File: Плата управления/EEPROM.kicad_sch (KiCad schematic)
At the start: 2 parts, among them U1 AT25xxx

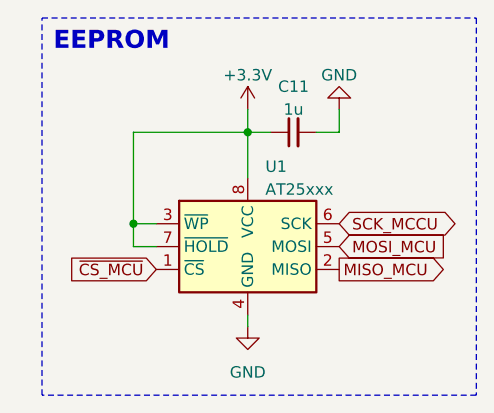
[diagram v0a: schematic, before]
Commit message: Заменил разъём под силовую плату
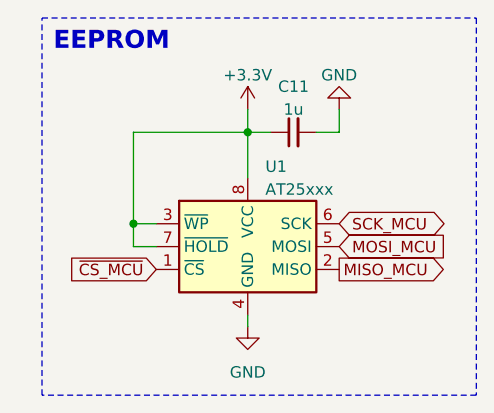
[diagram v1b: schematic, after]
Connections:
- net SCK_MCCU renamed SCK_MCU
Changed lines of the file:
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@@
     )
   )
-  (global_label "SCK_MCCU" (shape bidirectional) (at 48.26 38.1 0) (fields_autoplaced)
+  (global_label "SCK_MCU" (shape bidirectional) (at 48.26 38.1 0) (fields_autoplaced)
     (effects (font (size 1.27 1.27)) (justify left))
-    (property "Intersheetrefs" "${INTERSHEET_REFS}" (at 62.3161 38.1 0)
+    (property "Intersheetrefs" "${INTERSHEET_REFS}" (at 61.0461 38.1 0)
       (effects (font (size 1.27 1.27)) (justify left) hide)
     )

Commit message: Редактировал схему
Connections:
- net MISO_MCU renamed EEPROM_MISO_MCU
- net MOSI_MCU renamed EEPROM_MOSI_MCU
- net SCK_MCU renamed EEPROM_SCK_MCU
- net ~{CS_MCU} renamed EEPROM_~{CS_MCU}
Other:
- moved on the sheet: C11, U1
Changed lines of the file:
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@@
 (kicad_sch (version 20230121) (generator eeschema)
   (paper "A4")
-  (junction (at 25.4 38.1) (diameter 0) (color 0 0 0 0)
+  (junction (at 34.29 38.1) (diameter 0) (color 0 0 0 0)
   )
-  (junction (at 38.1 27.94) (diameter 0) (color 0 0 0 0)
+  (junction (at 46.99 27.94) (diameter 0) (color 0 0 0 0)
   )
-  (wire (pts (xy 38.1 33.02) (xy 38.1 27.94))
+  (wire (pts (xy 46.99 33.02) (xy 46.99 27.94))
     (stroke (width 0) (type default))
   )
-  (wire (pts (xy 25.4 27.94) (xy 38.1 27.94))
+  (wire (pts (xy 34.29 27.94) (xy 46.99 27.94))
     (stroke (width 0) (type default))
   )
-  (wire (pts (xy 38.1 27.94) (xy 40.64 27.94))
+  (wire (pts (xy 46.99 27.94) (xy 49.53 27.94))
     (stroke (width 0) (type default))
   )
-  (wire (pts (xy 38.1 25.4) (xy 38.1 27.94))
+  (wire (pts (xy 46.99 25.4) (xy 46.99 27.94))
     (stroke (width 0) (type default))
   )
-  (wire (pts (xy 45.72 27.94) (xy 48.26 27.94))
+  (wire (pts (xy 54.61 27.94) (xy 57.15 27.94))
     (stroke (width 0) (type default))
   )
-  (wire (pts (xy 25.4 40.64) (xy 25.4 38.1))
+  (wire (pts (xy 34.29 40.64) (xy 34.29 38.1))
     (stroke (width 0) (type default))
   )
-  (wire (pts (xy 27.94 40.64) (xy 25.4 40.64))
+  (wire (pts (xy 36.83 40.64) (xy 34.29 40.64))
     (stroke (width 0) (type default))
   )
-  (wire (pts (xy 25.4 38.1) (xy 27.94 38.1))
+  (wire (pts (xy 34.29 38.1) (xy 36.83 38.1))
     (stroke (width 0) (type default))
   )
-  (wire (pts (xy 25.4 38.1) (xy 25.4 27.94))
+  (wire (pts (xy 34.29 38.1) (xy 34.29 27.94))
     (stroke (width 0) (type default))
   )
-  (wire (pts (xy 38.1 48.26) (xy 38.1 49.53))
+  (wire (pts (xy 46.99 48.26) (xy 46.99 49.53))
     (stroke (width 0) (type default))
   )
-  (wire (pts (xy 48.26 27.94) (xy 48.26 25.4))
+  (wire (pts (xy 57.15 27.94) (xy 57.15 25.4))
     (stroke (width 0) (type default))
   )
-  (rectangle (start 15.24 15.24) (end 63.5 57.15)
+  (rectangle (start 15.24 15.24) (end 80.01 57.15)
     (stroke (width 0) (type dot))
     (fill (type none))
@@
     (effects (font (size 2 2) (thickness 0.4) bold) (justify left bottom))
   )
-  (global_label "MISO_MCU" (shape output) (at 48.26 43.18 0) (fields_autoplaced)
+  (global_label "EEPROM_MISO_MCU" (shape output) (at 57.15 43.18 0) (fields_autoplaced)
     (effects (font (size 1.27 1.27)) (justify left))
-    (property "Intersheetrefs" "${INTERSHEET_REFS}" (at 60.7815 43.18 0)
+    (property "Intersheetrefs" "${INTERSHEET_REFS}" (at 78.3384 43.18 0)
       (effects (font (size 1.27 1.27)) (justify left) hide)
     )
   )
-  (global_label "~{CS_MCU}" (shape input) (at 27.94 43.18 180) (fields_autoplaced)
+  (global_label "EEPROM_~{CS_MCU}" (shape input) (at 36.83 43.18 180) (fields_autoplaced)
     (effects (font (size 1.27 1.27)) (justify right))
-    (property "Intersheetrefs" "${INTERSHEET_REFS}" (at 17.5352 43.18 0)
+    (property "Intersheetrefs" "${INTERSHEET_REFS}" (at 17.7583 43.18 0)
       (effects (font (size 1.27 1.27)) (justify right) hide)
     )
   )
-  (global_label "SCK_MCU" (shape bidirectional) (at 48.26 38.1 0) (fields_autoplaced)
+  (global_label "EEPROM_SCK_MCU" (shape bidirectional) (at 57.15 38.1 0) (fields_autoplaced)
     (effects (font (size 1.27 1.27)) (justify left))
-    (property "Intersheetrefs" "${INTERSHEET_REFS}" (at 61.0461 38.1 0)
+    (property "Intersheetrefs" "${INTERSHEET_REFS}" (at 78.603 38.1 0)
       (effects (font (size 1.27 1.27)) (justify left) hide)
     )
   )
-  (global_label "MOSI_MCU" (shape input) (at 48.26 40.64 0) (fields_autoplaced)
+  (global_label "EEPROM_MOSI_MCU" (shape input) (at 57.15 40.64 0) (fields_autoplaced)
     (effects (font (size 1.27 1.27)) (justify left))
-    (property "Intersheetrefs" "${INTERSHEET_REFS}" (at 60.7815 40.64 0)
+    (property "Intersheetrefs" "${INTERSHEET_REFS}" (at 78.3384 40.64 0)
       (effects (font (size 1.27 1.27)) (justify left) hide)
     )
   )
-  (symbol (lib_id "Device:C_Small") (at 43.18 27.94 90) (unit 1)
+  (symbol (lib_id "Device:C_Small") (at 52.07 27.94 90) (unit 1)
     (in_bom yes) (on_board yes) (dnp no) (fields_autoplaced)
-    (property "Reference" "C11" (at 43.1863 22.86 90)
+    (property "Reference" "C11" (at 52.0763 22.86 90)
       (effects (font (size 1.27 1.27)))
     )
-    (property "Value" "1u" (at 43.1863 25.4 90)
+    (property "Value" "1u" (at 52.0763 25.4 90)
       (effects (font (size 1.27 1.27)))
     )
-    (property "Footprint" "Capacitor_SMD:C_0603_1608Metric_Pad1.08x0.95mm_HandSolder" (at 43.18 27.94 0)
+    (property "Footprint" "Capacitor_SMD:C_0603_1608Metric_Pad1.08x0.95mm_HandSolder" (at 52.07 27.94 0)
       (effects (font (size 1.27 1.27)) hide)
     )
-    (property "Datasheet" "~" (at 43.18 27.94 0)
+    (property "Datasheet" "~" (at 52.07 27.94 0)
       (effects (font (size 1.27 1.27)) hide)
     )
@@
     )
   )
-  (symbol (lib_id "power:GND") (at 38.1 49.53 0) (unit 1)
+  (symbol (lib_id "power:GND") (at 46.99 49.53 0) (unit 1)
     (in_bom yes) (on_board yes) (dnp no) (fields_autoplaced)
-    (property "Reference" "#PWR0108" (at 38.1 55.88 0)
+    (property "Reference" "#PWR0108" (at 46.99 55.88 0)
       (effects (font (size 1.27 1.27)) hide)
     )
-    (property "Value" "GND" (at 38.1 54.61 0)
+    (property "Value" "GND" (at 46.99 54.61 0)
       (effects (font (size 1.27 1.27)))
     )
-    (property "Footprint" "" (at 38.1 49.53 0)
+    (property "Footprint" "" (at 46.99 49.53 0)
       (effects (font (size 1.27 1.27)) hide)
     )
-    (property "Datasheet" "" (at 38.1 49.53 0)
+    (property "Datasheet" "" (at 46.99 49.53 0)
       (effects (font (size 1.27 1.27)) hide)
     )
@@
     )
   )
-  (symbol (lib_id "Memory_EEPROM:AT25xxx") (at 38.1 40.64 0) (unit 1)
+  (symbol (lib_id "Memory_EEPROM:AT25xxx") (at 46.99 40.64 0) (unit 1)
     (in_bom yes) (on_board yes) (dnp no) (fields_autoplaced)
-    (property "Reference" "U1" (at 40.0559 31.75 0)
+    (property "Reference" "U1" (at 48.9459 31.75 0)
       (effects (font (size 1.27 1.27)) (justify left))
     )
-    (property "Value" "AT25xxx" (at 40.0559 34.29 0)
+    (property "Value" "AT25xxx" (at 48.9459 34.29 0)
       (effects (font (size 1.27 1.27)) (justify left))
     )
-    (property "Footprint" "Package_SO:SOIC-8_3.9x4.9mm_P1.27mm" (at 38.1 40.64 0)
+    (property "Footprint" "Package_SO:SOIC-8_3.9x4.9mm_P1.27mm" (at 46.99 40.64 0)
       (effects (font (size 1.27 1.27)) hide)
     )
-    (property "Datasheet" "http://ww1.microchip.com/downloads/en/DeviceDoc/Atmel-8707-SEEPROM-AT25010B-020B-040B-Datasheet.pdf" (at 38.1 40.64 0)
+    (property "Datasheet" "http://ww1.microchip.com/downloads/en/DeviceDoc/Atmel-8707-SEEPROM-AT25010B-020B-040B-Datasheet.pdf" (at 46.99 40.64 0)
       (effects (font (size 1.27 1.27)) hide)
     )
@@
     )
   )
-  (symbol (lib_id "power:+3.3V") (at 38.1 25.4 0) (unit 1)
+  (symbol (lib_id "power:+3.3V") (at 46.99 25.4 0) (unit 1)
     (in_bom yes) (on_board yes) (dnp no) (fields_autoplaced)
-    (property "Reference" "#PWR0110" (at 38.1 29.21 0)
+    (property "Reference" "#PWR0110" (at 46.99 29.21 0)
       (effects (font (size 1.27 1.27)) hide)
     )
-    (property "Value" "+3.3V" (at 38.1 21.59 0)
+    (property "Value" "+3.3V" (at 46.99 21.59 0)
       (effects (font (size 1.27 1.27)))
     )
-    (property "Footprint" "" (at 38.1 25.4 0)
+    (property "Footprint" "" (at 46.99 25.4 0)
       (effects (font (size 1.27 1.27)) hide)
     )
-    (property "Datasheet" "" (at 38.1 25.4 0)
+    (property "Datasheet" "" (at 46.99 25.4 0)
       (effects (font (size 1.27 1.27)) hide)
     )
@@
     )
   )
-  (symbol (lib_id "power:GND") (at 48.26 25.4 180) (unit 1)
+  (symbol (lib_id "power:GND") (at 57.15 25.4 180) (unit 1)
     (in_bom yes) (on_board yes) (dnp no) (fields_autoplaced)
-    (property "Reference" "#PWR0109" (at 48.26 19.05 0)
+    (property "Reference" "#PWR0109" (at 57.15 19.05 0)
       (effects (font (size 1.27 1.27)) hide)
     )
-    (property "Value" "GND" (at 48.26 21.59 0)
+    (property "Value" "GND" (at 57.15 21.59 0)
       (effects (font (size 1.27 1.27)))
     )
-    (property "Footprint" "" (at 48.26 25.4 0)
+    (property "Footprint" "" (at 57.15 25.4 0)
       (effects (font (size 1.27 1.27)) hide)
     )
-    (property "Datasheet" "" (at 48.26 25.4 0)
+    (property "Datasheet" "" (at 57.15 25.4 0)
       (effects (font (size 1.27 1.27)) hide)
     )

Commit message: Собираю документацию
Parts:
- U1: value AT25xxx -> FM25W256
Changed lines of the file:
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@@
   (symbol (lib_id "Memory_EEPROM:AT25xxx") (at 46.99 40.64 0) (unit 1)
     (in_bom yes) (on_board yes) (dnp no) (fields_autoplaced)
-    (property "Reference" "U1" (at 48.9459 31.75 0)
+    (property "Reference" "U1" (at 49.1841 30.48 0)
       (effects (font (size 1.27 1.27)) (justify left))
     )
-    (property "Value" "AT25xxx" (at 48.9459 34.29 0)
+    (property "Value" "FM25W256" (at 49.1841 33.02 0)
       (effects (font (size 1.27 1.27)) (justify left))
     )

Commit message: Добавил документы
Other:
- note added: "FRAM"
- note removed: "EEPROM"
- moved on the sheet: C11, U1
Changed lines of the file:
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@@
 (kicad_sch (version 20230121) (generator eeschema)
   (paper "A4")
-  (junction (at 34.29 38.1) (diameter 0) (color 0 0 0 0)
+  (title_block
+    (comment 1 "МПСТ.76721.758764.02.Э3.М")
   )
-  (junction (at 46.99 27.94) (diameter 0) (color 0 0 0 0)
+  (junction (at 147.955 103.505) (diameter 0) (color 0 0 0 0)
   )
-  (wire (pts (xy 46.99 33.02) (xy 46.99 27.94))
+  (junction (at 160.655 93.345) (diameter 0) (color 0 0 0 0)
+  )
+  (wire (pts (xy 160.655 98.425) (xy 160.655 93.345))
     (stroke (width 0) (type default))
   )
-  (wire (pts (xy 34.29 27.94) (xy 46.99 27.94))
+  (wire (pts (xy 147.955 93.345) (xy 160.655 93.345))
     (stroke (width 0) (type default))
   )
-  (wire (pts (xy 46.99 27.94) (xy 49.53 27.94))
+  (wire (pts (xy 160.655 93.345) (xy 163.195 93.345))
     (stroke (width 0) (type default))
   )
-  (wire (pts (xy 46.99 25.4) (xy 46.99 27.94))
+  (wire (pts (xy 160.655 90.805) (xy 160.655 93.345))
     (stroke (width 0) (type default))
   )
-  (wire (pts (xy 54.61 27.94) (xy 57.15 27.94))
+  (wire (pts (xy 168.275 93.345) (xy 170.815 93.345))
     (stroke (width 0) (type default))
   )
-  (wire (pts (xy 34.29 40.64) (xy 34.29 38.1))
+  (wire (pts (xy 147.955 106.045) (xy 147.955 103.505))
     (stroke (width 0) (type default))
   )
-  (wire (pts (xy 36.83 40.64) (xy 34.29 40.64))
+  (wire (pts (xy 150.495 106.045) (xy 147.955 106.045))
     (stroke (width 0) (type default))
   )
-  (wire (pts (xy 34.29 38.1) (xy 36.83 38.1))
+  (wire (pts (xy 147.955 103.505) (xy 150.495 103.505))
     (stroke (width 0) (type default))
   )
-  (wire (pts (xy 34.29 38.1) (xy 34.29 27.94))
+  (wire (pts (xy 147.955 103.505) (xy 147.955 93.345))
     (stroke (width 0) (type default))
   )
-  (wire (pts (xy 46.99 48.26) (xy 46.99 49.53))
+  (wire (pts (xy 160.655 113.665) (xy 160.655 114.935))
     (stroke (width 0) (type default))
   )
-  (wire (pts (xy 57.15 27.94) (xy 57.15 25.4))
+  (wire (pts (xy 170.815 93.345) (xy 170.815 90.805))
     (stroke (width 0) (type default))
   )
-  (rectangle (start 15.24 15.24) (end 80.01 57.15)
-    (stroke (width 0) (type dot))
+  (rectangle (start 128.905 80.645) (end 193.675 122.555)
+    (stroke (width 0) (type dash))
     (fill (type none))
   )
-  (text "EEPROM" (at 16.51 19.05 0)
+  (text "FRAM" (at 130.175 84.455 0)
     (effects (font (size 2 2) (thickness 0.4) bold) (justify left bottom))
   )
-  (global_label "EEPROM_MISO_MCU" (shape output) (at 57.15 43.18 0) (fields_autoplaced)
+  (global_label "EEPROM_MISO_MCU" (shape output) (at 170.815 108.585 0) (fields_autoplaced)
     (effects (font (size 1.27 1.27)) (justify left))
-    (property "Intersheetrefs" "${INTERSHEET_REFS}" (at 78.3384 43.18 0)
+    (property "Intersheetrefs" "${INTERSHEET_REFS}" (at 192.0034 108.585 0)
       (effects (font (size 1.27 1.27)) (justify left) hide)
     )
   )
-  (global_label "EEPROM_~{CS_MCU}" (shape input) (at 36.83 43.18 180) (fields_autoplaced)
+  (global_label "EEPROM_~{CS_MCU}" (shape input) (at 150.495 108.585 180) (fields_autoplaced)
     (effects (font (size 1.27 1.27)) (justify right))
-    (property "Intersheetrefs" "${INTERSHEET_REFS}" (at 17.7583 43.18 0)
+    (property "Intersheetrefs" "${INTERSHEET_REFS}" (at 131.4233 108.585 0)
       (effects (font (size 1.27 1.27)) (justify right) hide)
     )
   )
-  (global_label "EEPROM_SCK_MCU" (shape bidirectional) (at 57.15 38.1 0) (fields_autoplaced)
+  (global_label "EEPROM_SCK_MCU" (shape bidirectional) (at 170.815 103.505 0) (fields_autoplaced)
     (effects (font (size 1.27 1.27)) (justify left))
-    (property "Intersheetrefs" "${INTERSHEET_REFS}" (at 78.603 38.1 0)
+    (property "Intersheetrefs" "${INTERSHEET_REFS}" (at 192.268 103.505 0)
       (effects (font (size 1.27 1.27)) (justify left) hide)
     )
   )
-  (global_label "EEPROM_MOSI_MCU" (shape input) (at 57.15 40.64 0) (fields_autoplaced)
+  (global_label "EEPROM_MOSI_MCU" (shape input) (at 170.815 106.045 0) (fields_autoplaced)
     (effects (font (size 1.27 1.27)) (justify left))
-    (property "Intersheetrefs" "${INTERSHEET_REFS}" (at 78.3384 40.64 0)
+    (property "Intersheetrefs" "${INTERSHEET_REFS}" (at 192.0034 106.045 0)
       (effects (font (size 1.27 1.27)) (justify left) hide)
     )
   )
-  (symbol (lib_id "Device:C_Small") (at 52.07 27.94 90) (unit 1)
+  (symbol (lib_id "Device:C_Small") (at 165.735 93.345 90) (unit 1)
     (in_bom yes) (on_board yes) (dnp no) (fields_autoplaced)
-    (property "Reference" "C11" (at 52.0763 22.86 90)
+    (property "Reference" "C11" (at 165.7413 88.265 90)
       (effects (font (size 1.27 1.27)))
     )
-    (property "Value" "1u" (at 52.0763 25.4 90)
+    (property "Value" "1u" (at 165.7413 90.805 90)
       (effects (font (size 1.27 1.27)))
     )
-    (property "Footprint" "Capacitor_SMD:C_0603_1608Metric_Pad1.08x0.95mm_HandSolder" (at 52.07 27.94 0)
+    (property "Footprint" "Capacitor_SMD:C_0603_1608Metric_Pad1.08x0.95mm_HandSolder" (at 165.735 93.345 0)
       (effects (font (size 1.27 1.27)) hide)
     )
-    (property "Datasheet" "~" (at 52.07 27.94 0)
+    (property "Datasheet" "~" (at 165.735 93.345 0)
       (effects (font (size 1.27 1.27)) hide)
     )
@@
     )
   )
-  (symbol (lib_id "power:GND") (at 46.99 49.53 0) (unit 1)
+  (symbol (lib_id "power:GND") (at 160.655 114.935 0) (unit 1)
     (in_bom yes) (on_board yes) (dnp no) (fields_autoplaced)
-    (property "Reference" "#PWR0108" (at 46.99 55.88 0)
+    (property "Reference" "#PWR0108" (at 160.655 121.285 0)
       (effects (font (size 1.27 1.27)) hide)
     )
-    (property "Value" "GND" (at 46.99 54.61 0)
+    (property "Value" "GND" (at 160.655 120.015 0)
       (effects (font (size 1.27 1.27)))
     )
-    (property "Footprint" "" (at 46.99 49.53 0)
+    (property "Footprint" "" (at 160.655 114.935 0)
       (effects (font (size 1.27 1.27)) hide)
     )
-    (property "Datasheet" "" (at 46.99 49.53 0)
+    (property "Datasheet" "" (at 160.655 114.935 0)
       (effects (font (size 1.27 1.27)) hide)
     )
@@
     )
   )
-  (symbol (lib_id "Memory_EEPROM:AT25xxx") (at 46.99 40.64 0) (unit 1)
+  (symbol (lib_id "Memory_EEPROM:AT25xxx") (at 160.655 106.045 0) (unit 1)
     (in_bom yes) (on_board yes) (dnp no) (fields_autoplaced)
-    (property "Reference" "U1" (at 49.1841 30.48 0)
+    (property "Reference" "U1" (at 162.8491 95.885 0)
       (effects (font (size 1.27 1.27)) (justify left))
     )
-    (property "Value" "FM25W256" (at 49.1841 33.02 0)
+    (property "Value" "FM25W256" (at 162.8491 98.425 0)
       (effects (font (size 1.27 1.27)) (justify left))
     )
-    (property "Footprint" "Package_SO:SOIC-8_3.9x4.9mm_P1.27mm" (at 46.99 40.64 0)
+    (property "Footprint" "Package_SO:SOIC-8_3.9x4.9mm_P1.27mm" (at 160.655 106.045 0)
       (effects (font (size 1.27 1.27)) hide)
     )
-    (property "Datasheet" "http://ww1.microchip.com/downloads/en/DeviceDoc/Atmel-8707-SEEPROM-AT25010B-020B-040B-Datasheet.pdf" (at 46.99 40.64 0)
+    (property "Datasheet" "http://ww1.microchip.com/downloads/en/DeviceDoc/Atmel-8707-SEEPROM-AT25010B-020B-040B-Datasheet.pdf" (at 160.655 106.045 0)
       (effects (font (size 1.27 1.27)) hide)
     )
@@
     )
   )
-  (symbol (lib_id "power:+3.3V") (at 46.99 25.4 0) (unit 1)
+  (symbol (lib_id "power:+3.3V") (at 160.655 90.805 0) (unit 1)
     (in_bom yes) (on_board yes) (dnp no) (fields_autoplaced)
-    (property "Reference" "#PWR0110" (at 46.99 29.21 0)
+    (property "Reference" "#PWR0110" (at 160.655 94.615 0)
       (effects (font (size 1.27 1.27)) hide)
     )
-    (property "Value" "+3.3V" (at 46.99 21.59 0)
+    (property "Value" "+3.3V" (at 160.655 86.995 0)
       (effects (font (size 1.27 1.27)))
     )
-    (property "Footprint" "" (at 46.99 25.4 0)
+    (property "Footprint" "" (at 160.655 90.805 0)
       (effects (font (size 1.27 1.27)) hide)
     )
-    (property "Datasheet" "" (at 46.99 25.4 0)
+    (property "Datasheet" "" (at 160.655 90.805 0)
       (effects (font (size 1.27 1.27)) hide)
     )
@@
     )
   )
-  (symbol (lib_id "power:GND") (at 57.15 25.4 180) (unit 1)
+  (symbol (lib_id "power:GND") (at 170.815 90.805 180) (unit 1)
     (in_bom yes) (on_board yes) (dnp no) (fields_autoplaced)
-    (property "Reference" "#PWR0109" (at 57.15 19.05 0)
+    (property "Reference" "#PWR0109" (at 170.815 84.455 0)
       (effects (font (size 1.27 1.27)) hide)
     )
-    (property "Value" "GND" (at 57.15 21.59 0)
+    (property "Value" "GND" (at 170.815 86.995 0)
       (effects (font (size 1.27 1.27)))
     )
-    (property "Footprint" "" (at 57.15 25.4 0)
+    (property "Footprint" "" (at 170.815 90.805 0)
       (effects (font (size 1.27 1.27)) hide)
     )
-    (property "Datasheet" "" (at 57.15 25.4 0)
+    (property "Datasheet" "" (at 170.815 90.805 0)
       (effects (font (size 1.27 1.27)) hide)
     )

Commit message: Добавил все документы
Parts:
- renumbered C11 to C54, U1 to U12
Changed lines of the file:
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@@
   (symbol (lib_id "Device:C_Small") (at 165.735 93.345 90) (unit 1)
     (in_bom yes) (on_board yes) (dnp no) (fields_autoplaced)
-    (property "Reference" "C11" (at 165.7413 88.265 90)
+    (property "Reference" "C54" (at 165.7413 88.265 90)
       (effects (font (size 1.27 1.27)))
     )
@@
       (project "Плата управления"
         (path "/75f4c67c-bbde-4446-8f82-67797a1b269f/bbae964f-aef3-47b6-89c5-594b5cc7787c"
-          (reference "C11") (unit 1)
+          (reference "C54") (unit 1)
         )
       )
@@
   (symbol (lib_id "power:GND") (at 160.655 114.935 0) (unit 1)
     (in_bom yes) (on_board yes) (dnp no) (fields_autoplaced)
-    (property "Reference" "#PWR0108" (at 160.655 121.285 0)
+    (property "Reference" "#PWR0104" (at 160.655 121.285 0)
       (effects (font (size 1.27 1.27)) hide)
     )
@@
       (project "Плата управления"
         (path "/75f4c67c-bbde-4446-8f82-67797a1b269f/bbae964f-aef3-47b6-89c5-594b5cc7787c"
-          (reference "#PWR0108") (unit 1)
+          (reference "#PWR0104") (unit 1)
         )
       )
@@
   (symbol (lib_id "Memory_EEPROM:AT25xxx") (at 160.655 106.045 0) (unit 1)
     (in_bom yes) (on_board yes) (dnp no) (fields_autoplaced)
-    (property "Reference" "U1" (at 162.8491 95.885 0)
+    (property "Reference" "U12" (at 162.8491 95.885 0)
       (effects (font (size 1.27 1.27)) (justify left))
     )
@@
       (project "Плата управления"
         (path "/75f4c67c-bbde-4446-8f82-67797a1b269f/bbae964f-aef3-47b6-89c5-594b5cc7787c"
-          (reference "U1") (unit 1)
+          (reference "U12") (unit 1)
         )
       )
@@
   (symbol (lib_id "power:+3.3V") (at 160.655 90.805 0) (unit 1)
     (in_bom yes) (on_board yes) (dnp no) (fields_autoplaced)
-    (property "Reference" "#PWR0110" (at 160.655 94.615 0)
+    (property "Reference" "#PWR0102" (at 160.655 94.615 0)
       (effects (font (size 1.27 1.27)) hide)
     )
@@
       (project "Плата управления"
         (path "/75f4c67c-bbde-4446-8f82-67797a1b269f/bbae964f-aef3-47b6-89c5-594b5cc7787c"
-          (reference "#PWR0110") (unit 1)
+          (reference "#PWR0102") (unit 1)
         )
       )
@@
   (symbol (lib_id "power:GND") (at 170.815 90.805 180) (unit 1)
     (in_bom yes) (on_board yes) (dnp no) (fields_autoplaced)
-    (property "Reference" "#PWR0109" (at 170.815 84.455 0)
+    (property "Reference" "#PWR0103" (at 170.815 84.455 0)
       (effects (font (size 1.27 1.27)) hide)
     )
@@
       (project "Плата управления"
         (path "/75f4c67c-bbde-4446-8f82-67797a1b269f/bbae964f-aef3-47b6-89c5-594b5cc7787c"
-          (reference "#PWR0109") (unit 1)
+          (reference "#PWR0103") (unit 1)
         )
       )

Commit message: Версия под отчёт
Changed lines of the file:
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@@
     (fill (type none))
   )
-  (text "FRAM" (at 130.175 84.455 0)
-    (effects (font (size 2 2) (thickness 0.4) bold) (justify left bottom))
+  (text "FRAM" (at 157.48 80.01 0)
+    (effects (font (size 2.5 2.5) (thickness 0.4) bold) (justify left bottom))
   )
   (global_label "EEPROM_MISO_MCU" (shape output) (at 170.815 108.585 0) (fields_autoplaced)
